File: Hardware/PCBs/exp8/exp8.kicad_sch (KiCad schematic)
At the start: 5 parts, among them J1 Conn_01x07_Female, J2 Conn_01x02_Female, U1 7410, U2 7410, U3 7400

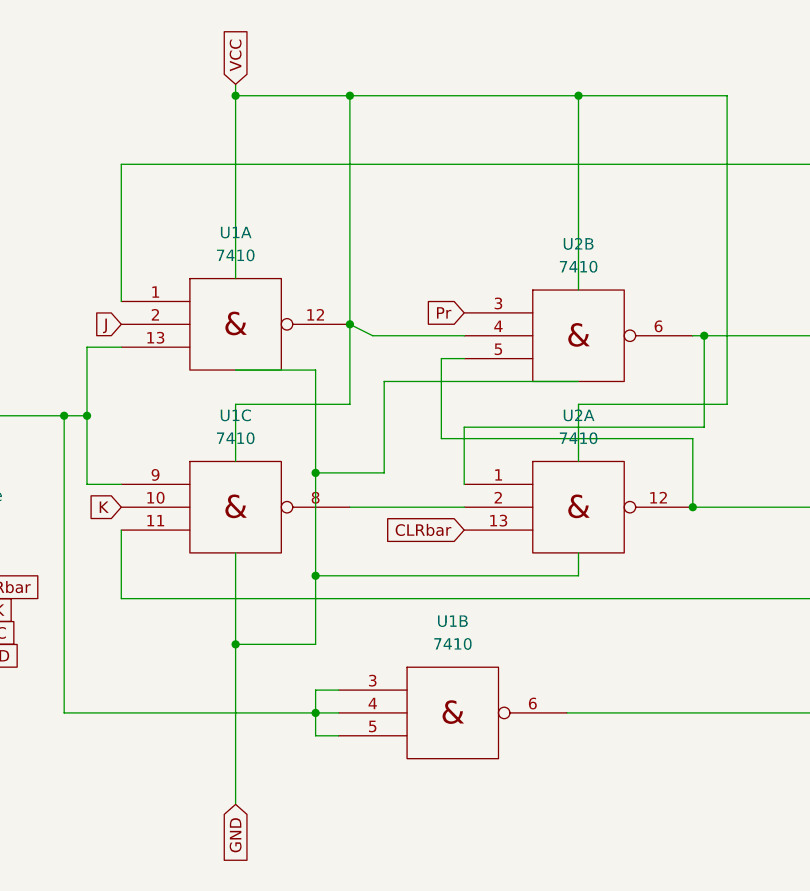
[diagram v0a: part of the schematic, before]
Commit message: Several PCBs updated
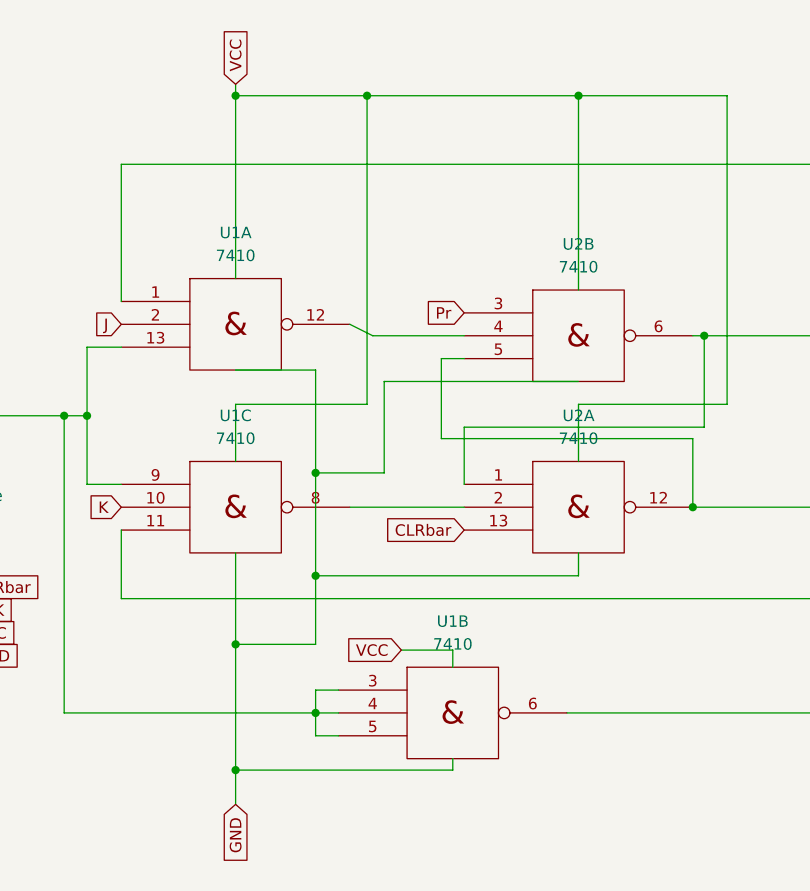
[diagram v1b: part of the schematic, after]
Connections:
- net Vcc: no longer U1.12, U2.4
- new net: U1.12, U2.4
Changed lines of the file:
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@@
   (junction (at 38.1 57.15) (diameter 0) (color 0 0 0 0)
   )
-  (junction (at 69.85 46.99) (diameter 0) (color 0 0 0 0)
-  )
   (junction (at 170.18 66.04) (diameter 0) (color 0 0 0 0)
   )
   (junction (at 57.15 21.59) (diameter 0) (color 0 0 0 0)
   )
+  (junction (at 71.755 21.59) (diameter 0) (color 0 0 0 0)
+  )
   (junction (at 40.64 57.15) (diameter 0) (color 0 0 0 0)
   )
@@
   (junction (at 139.7 64.77) (diameter 0) (color 0 0 0 0)
   )
+  (junction (at 57.15 96.52) (diameter 0) (color 0 0 0 0)
+  )
   (junction (at 107.95 67.31) (diameter 0) (color 0 0 0 0)
   )
   (junction (at 171.45 50.8) (diameter 0) (color 0 0 0 0)
   )
-  (junction (at 69.85 21.59) (diameter 0) (color 0 0 0 0)
-  )
   (junction (at 95.25 21.59) (diameter 0) (color 0 0 0 0)
   )
   (junction (at 193.04 48.26) (diameter 0) (color 0 0 0 0)
   )
-  (wire (pts (xy 69.85 55.88) (xy 69.85 46.99))
-    (stroke (width 0) (type default) (color 0 0 0 0))
-  )
   (wire (pts (xy 57.15 82.55) (xy 66.04 82.55))
     (stroke (width 0) (type default) (color 0 0 0 0))
@@
     (stroke (width 0) (type default) (color 0 0 0 0))
   )
+  (wire (pts (xy 57.15 21.59) (xy 71.755 21.59))
+    (stroke (width 0) (type default) (color 0 0 0 0))
+  )
   (wire (pts (xy 95.25 72.39) (xy 95.25 74.93))
     (stroke (width 0) (type default) (color 0 0 0 0))
@@
     (stroke (width 0) (type default) (color 0 0 0 0))
   )
-  (wire (pts (xy 95.25 21.59) (xy 69.85 21.59))
-    (stroke (width 0) (type default) (color 0 0 0 0))
-  )
-  (wire (pts (xy 57.15 55.88) (xy 69.85 55.88))
+  (wire (pts (xy 95.25 21.59) (xy 71.755 21.59))
+    (stroke (width 0) (type default) (color 0 0 0 0))
+  )
+  (wire (pts (xy 57.15 55.88) (xy 71.755 55.88))
     (stroke (width 0) (type default) (color 0 0 0 0))
   )
@@
     (stroke (width 0) (type default) (color 0 0 0 0))
   )
+  (wire (pts (xy 75.565 83.185) (xy 81.28 83.185))
+    (stroke (width 0) (type default) (color 0 0 0 0))
+  )
   (wire (pts (xy 168.91 48.26) (xy 168.91 45.72))
     (stroke (width 0) (type default) (color 0 0 0 0))
@@
     (stroke (width 0) (type default) (color 0 0 0 0))
   )
-  (wire (pts (xy 57.15 82.55) (xy 57.15 100.33))
+  (wire (pts (xy 57.15 82.55) (xy 57.15 96.52))
     (stroke (width 0) (type default) (color 0 0 0 0))
   )
@@
     (stroke (width 0) (type default) (color 0 0 0 0))
   )
+  (wire (pts (xy 57.15 96.52) (xy 57.15 100.33))
+    (stroke (width 0) (type default) (color 0 0 0 0))
+  )
   (wire (pts (xy 109.22 48.26) (xy 128.27 48.26))
     (stroke (width 0) (type default) (color 0 0 0 0))
@@
     (stroke (width 0) (type default) (color 0 0 0 0))
   )
-  (wire (pts (xy 69.85 46.99) (xy 69.85 21.59))
+  (wire (pts (xy 71.755 21.59) (xy 71.755 55.88))
     (stroke (width 0) (type default) (color 0 0 0 0))
   )
@@
     (stroke (width 0) (type default) (color 0 0 0 0))
   )
+  (wire (pts (xy 81.28 95.25) (xy 81.28 96.52))
+    (stroke (width 0) (type default) (color 0 0 0 0))
+  )
   (wire (pts (xy 66.04 74.93) (xy 66.04 82.55))
     (stroke (width 0) (type default) (color 0 0 0 0))
@@
     (stroke (width 0) (type default) (color 0 0 0 0))
   )
+  (wire (pts (xy 81.28 83.185) (xy 81.28 85.09))
+    (stroke (width 0) (type default) (color 0 0 0 0))
+  )
   (wire (pts (xy 66.04 87.63) (xy 66.04 90.17))
     (stroke (width 0) (type default) (color 0 0 0 0))
@@
     (stroke (width 0) (type default) (color 0 0 0 0))
   )
-  (wire (pts (xy 69.85 21.59) (xy 57.15 21.59))
+  (wire (pts (xy 81.28 96.52) (xy 57.15 96.52))
     (stroke (width 0) (type default) (color 0 0 0 0))
   )
@@
       (effects (font (size 1.27 1.27)) (justify right) hide)
     )
+  )
+  (global_label "VCC" (shape input) (at 75.565 83.185 180) (fields_autoplaced)
+    (effects (font (size 1.27 1.27)) (justify right))
+    (property "Intersheet References" "${INTERSHEET_REFS}" (id 0) (at 69.5233 83.1056 0)
+      (effects (font (size 1.27 1.27)) (justify right) hide)
+    )

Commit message: Multiple PCBs updated
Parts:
- added H1, H2, H3, H4: MountingHole, MountingHole:MountingHole_2.5mm, symbol Mechanical:MountingHole
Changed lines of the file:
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@@
   (junction (at 57.15 21.59) (diameter 0) (color 0 0 0 0)
   )
-  (junction (at 71.755 21.59) (diameter 0) (color 0 0 0 0)
-  )
   (junction (at 40.64 57.15) (diameter 0) (color 0 0 0 0)
   )
@@
   (junction (at 139.7 64.77) (diameter 0) (color 0 0 0 0)
   )
-  (junction (at 57.15 96.52) (diameter 0) (color 0 0 0 0)
-  )
   (junction (at 107.95 67.31) (diameter 0) (color 0 0 0 0)
   )
   (junction (at 171.45 50.8) (diameter 0) (color 0 0 0 0)
   )
+  (junction (at 69.85 21.59) (diameter 0) (color 0 0 0 0)
+  )
   (junction (at 95.25 21.59) (diameter 0) (color 0 0 0 0)
   )
@@
     (stroke (width 0) (type default) (color 0 0 0 0))
   )
-  (wire (pts (xy 57.15 21.59) (xy 71.755 21.59))
-    (stroke (width 0) (type default) (color 0 0 0 0))
-  )
   (wire (pts (xy 95.25 72.39) (xy 95.25 74.93))
     (stroke (width 0) (type default) (color 0 0 0 0))
@@
     (stroke (width 0) (type default) (color 0 0 0 0))
   )
-  (wire (pts (xy 95.25 21.59) (xy 71.755 21.59))
-    (stroke (width 0) (type default) (color 0 0 0 0))
-  )
-  (wire (pts (xy 57.15 55.88) (xy 71.755 55.88))
+  (wire (pts (xy 95.25 21.59) (xy 69.85 21.59))
+    (stroke (width 0) (type default) (color 0 0 0 0))
+  )
+  (wire (pts (xy 57.15 55.88) (xy 69.85 55.88))
     (stroke (width 0) (type default) (color 0 0 0 0))
   )
@@
     (stroke (width 0) (type default) (color 0 0 0 0))
   )
-  (wire (pts (xy 75.565 83.185) (xy 81.28 83.185))
-    (stroke (width 0) (type default) (color 0 0 0 0))
-  )
   (wire (pts (xy 168.91 48.26) (xy 168.91 45.72))
     (stroke (width 0) (type default) (color 0 0 0 0))
@@
     (stroke (width 0) (type default) (color 0 0 0 0))
   )
-  (wire (pts (xy 57.15 82.55) (xy 57.15 96.52))
+  (wire (pts (xy 57.15 82.55) (xy 57.15 100.33))
     (stroke (width 0) (type default) (color 0 0 0 0))
   )
@@
     (stroke (width 0) (type default) (color 0 0 0 0))
   )
-  (wire (pts (xy 57.15 96.52) (xy 57.15 100.33))
-    (stroke (width 0) (type default) (color 0 0 0 0))
-  )
   (wire (pts (xy 109.22 48.26) (xy 128.27 48.26))
     (stroke (width 0) (type default) (color 0 0 0 0))
@@
     (stroke (width 0) (type default) (color 0 0 0 0))
   )
-  (wire (pts (xy 71.755 21.59) (xy 71.755 55.88))
+  (wire (pts (xy 69.85 21.59) (xy 69.85 55.88))
     (stroke (width 0) (type default) (color 0 0 0 0))
   )
@@
     (stroke (width 0) (type default) (color 0 0 0 0))
   )
-  (wire (pts (xy 81.28 95.25) (xy 81.28 96.52))
-    (stroke (width 0) (type default) (color 0 0 0 0))
-  )
   (wire (pts (xy 66.04 74.93) (xy 66.04 82.55))
     (stroke (width 0) (type default) (color 0 0 0 0))
@@
     (stroke (width 0) (type default) (color 0 0 0 0))
   )
-  (wire (pts (xy 81.28 83.185) (xy 81.28 85.09))
-    (stroke (width 0) (type default) (color 0 0 0 0))
-  )
   (wire (pts (xy 66.04 87.63) (xy 66.04 90.17))
     (stroke (width 0) (type default) (color 0 0 0 0))
@@
     (stroke (width 0) (type default) (color 0 0 0 0))
   )
-  (wire (pts (xy 81.28 96.52) (xy 57.15 96.52))
+  (wire (pts (xy 69.85 21.59) (xy 57.15 21.59))
     (stroke (width 0) (type default) (color 0 0 0 0))
   )
@@
     )
   )
-  (global_label "VCC" (shape input) (at 75.565 83.185 180) (fields_autoplaced)
-    (effects (font (size 1.27 1.27)) (justify right))
-    (property "Intersheet References" "${INTERSHEET_REFS}" (id 0) (at 69.5233 83.1056 0)
-      (effects (font (size 1.27 1.27)) (justify right) hide)
-    )
-  )
   (global_label "Pr" (shape input) (at 82.55 45.72 180) (fields_autoplaced)
     (effects (font (size 1.27 1.27)) (justify right))
@@
     )
   )
+  (global_label "GND" (shape input) (at 81.28 95.25 270) (fields_autoplaced)
+    (effects (font (size 1.27 1.27)) (justify right))
+    (property "Intersheet References" "${INTERSHEET_REFS}" (id 0) (at 81.3594 101.5336 90)
+      (effects (font (size 1.27 1.27)) (justify right) hide)
+    )
+  )
   (global_label "CLK" (shape input) (at 26.67 78.74 0) (fields_autoplaced)
     (effects (font (size 1.27 1.27)) (justify left))
@@
     (effects (font (size 1.27 1.27)) (justify left))
     (property "Intersheet References" "${INTERSHEET_REFS}" (id 0) (at 32.9536 83.7406 0)
+      (effects (font (size 1.27 1.27)) (justify left) hide)
+    )
+  )
+  (global_label "VCC" (shape input) (at 81.28 85.09 90) (fields_autoplaced)
+    (effects (font (size 1.27 1.27)) (justify left))
+    (property "Intersheet References" "${INTERSHEET_REFS}" (id 0) (at 81.3594 79.0483 90)
       (effects (font (size 1.27 1.27)) (justify left) hide)
     )
@@
     (pin "9")
   )
+  (symbol (lib_id "Mechanical:MountingHole") (at 200.66 38.1 0) (unit 1)
+    (in_bom yes) (on_board yes) (fields_autoplaced)
+    (property "Reference" "H4" (id 0) (at 203.2 36.8299 0)
+      (effects (font (size 1.27 1.27)) (justify left))
+    )
+    (property "Value" "MountingHole" (id 1) (at 203.2 39.3699 0)
+      (effects (font (size 1.27 1.27)) (justify left))
+    )
+    (property "Footprint" "MountingHole:MountingHole_2.5mm" (id 2) (at 200.66 38.1 0)
+      (effects (font (size 1.27 1.27)) hide)
+    )
+    (property "Datasheet" "~" (id 3) (at 200.66 38.1 0)
+      (effects (font (size 1.27 1.27)) hide)
+    )
+  )
   (symbol (lib_id "74xx_IEEE:7410") (at 81.28 90.17 0) (unit 2)
     (in_bom yes) (on_board yes) (fields_autoplaced)
@@
     (pin "9")
   )
+  (symbol (lib_id "Mechanical:MountingHole") (at 199.39 30.48 0) (unit 1)
+    (in_bom yes) (on_board yes) (fields_autoplaced)
+    (property "Reference" "H3" (id 0) (at 201.93 29.2099 0)
+      (effects (font (size 1.27 1.27)) (justify left))
+    )
+    (property "Value" "MountingHole" (id 1) (at 201.93 31.7499 0)
+      (effects (font (size 1.27 1.27)) (justify left))
+    )
+    (property "Footprint" "MountingHole:MountingHole_2.5mm" (id 2) (at 199.39 30.48 0)
+      (effects (font (size 1.27 1.27)) hide)
+    )
+    (property "Datasheet" "~" (id 3) (at 199.39 30.48 0)
+      (effects (font (size 1.27 1.27)) hide)
+    )
+  )
   (symbol (lib_id "74xx_IEEE:7410") (at 57.15 67.31 0) (unit 3)
     (in_bom yes) (on_board yes) (fields_autoplaced)
@@
     (pin "9")
   )
+  (symbol (lib_id "Mechanical:MountingHole") (at 186.69 30.48 0) (unit 1)
+    (in_bom yes) (on_board yes) (fields_autoplaced)
+    (property "Reference" "H1" (id 0) (at 189.23 29.2099 0)
+      (effects (font (size 1.27 1.27)) (justify left))
+    )
+    (property "Value" "MountingHole" (id 1) (at 189.23 31.7499 0)
+      (effects (font (size 1.27 1.27)) (justify left))
+    )
+    (property "Footprint" "MountingHole:MountingHole_2.5mm" (id 2) (at 186.69 30.48 0)
+      (effects (font (size 1.27 1.27)) hide)
+    )
+    (property "Datasheet" "~" (id 3) (at 186.69 30.48 0)
+      (effects (font (size 1.27 1.27)) hide)
+    )
+  )
+  (symbol (lib_id "Mechanical:MountingHole") (at 191.77 38.1 0) (unit 1)
+    (in_bom yes) (on_board yes) (fields_autoplaced)
+    (property "Reference" "H2" (id 0) (at 194.31 36.8299 0)
+      (effects (font (size 1.27 1.27)) (justify left))
+    )
+    (property "Value" "MountingHole" (id 1) (at 194.31 39.3699 0)
+      (effects (font (size 1.27 1.27)) (justify left))
+    )
+    (property "Footprint" "MountingHole:MountingHole_2.5mm" (id 2) (at 191.77 38.1 0)
+      (effects (font (size 1.27 1.27)) hide)
+    )
+    (property "Datasheet" "~" (id 3) (at 191.77 38.1 0)
+      (effects (font (size 1.27 1.27)) hide)
+    )
+  )
   (symbol (lib_id "Connector:Conn_01x02_Female") (at 217.17 57.15 0) (unit 1)
     (in_bom yes) (on_board yes) (fields_autoplaced)
@@
   )
   (symbol_instances
+    (path "/e8dbad7f-08bc-4307-b227-743b5f751e25"
+      (reference "H1") (unit 1) (value "MountingHole") (footprint "MountingHole:MountingHole_2.5mm")
+    )
+    (path "/ef6dab83-86bf-4aba-8127-346d4bcc6ae0"
+      (reference "H2") (unit 1) (value "MountingHole") (footprint "MountingHole:MountingHole_2.5mm")
+    )
+    (path "/d43c6ed1-d232-4ca9-b1b2-324125d9a43a"
+      (reference "H3") (unit 1) (value "MountingHole") (footprint "MountingHole:MountingHole_2.5mm")
+    )
+    (path "/8f8079cd-136d-4c81-a301-fc26834d928c"
+      (reference "H4") (unit 1) (value "MountingHole") (footprint "MountingHole:MountingHole_2.5mm")
+    )
     (path "/64d1db30-7931-4980-9a73-3694b40a474f"
       (reference "J1") (unit 1) (value "Conn_01x07_Female") (footprint "Connector_JST:JST_EH_S7B-EH_1x07_P2.50mm_Horizontal")
